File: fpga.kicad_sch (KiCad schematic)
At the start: 0 parts

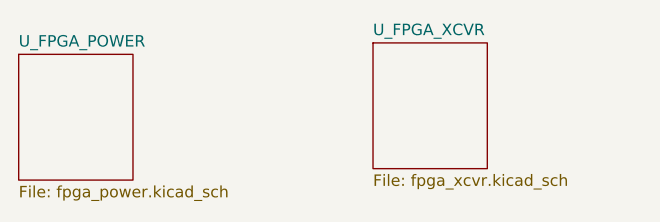
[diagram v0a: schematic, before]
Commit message: develop: Deleted FPGA_XCVR because there are no xcvrs on this part. Updated symbol.
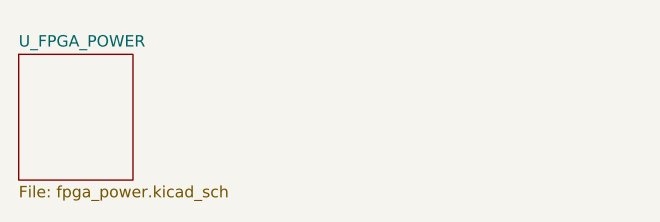
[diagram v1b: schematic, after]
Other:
- removed sheet U_FPGA_XCVR
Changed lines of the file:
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@@
-		)
-	)
-	(sheet
-		(at 95.25 62.23)
-		(size 12.7 13.97)
-		(exclude_from_sim no)
-		(in_bom yes)
-		(on_board yes)
-		(dnp no)
-		(fields_autoplaced yes)
-		(stroke
-			(width 0.1524)
-			(type solid)
-		)
-		(fill
-			(color 0 0 0 0.0000)
-		)
-		(property "Sheetname" "U_FPGA_XCVR"
-			(at 95.25 61.5184 0)
-			(effects
-				(font
-					(size 1.27 1.27)
-				)
-				(justify left bottom)
-			)
-		)
-		(property "Sheetfile" "fpga_xcvr.kicad_sch"
-			(at 95.25 76.7846 0)
-			(effects
-				(font
-					(size 1.27 1.27)
-				)
-				(justify left top)
-			)
-		)
-		(instances
-			(project "duality"
-				(path "/ba4aeeea-982a-4252-9638-c2cfeb24b844/e7ec6ff6-6367-4e7f-b7f8-4850ee864d63"
-					(page "7")
-				)
-			)
 		)
 	)
